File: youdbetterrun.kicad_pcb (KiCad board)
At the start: 4 copper layers, 60 x 53 mm, 51 parts, among them J1 GT-USB-7010ASV, J2 Conn_01x05_Pin, J3 Conn_01x10_Pin, J4 FH12A-24S-0.5SH(55), Q1 S8050, Q2 S8050, Q3 Q_NMOS_GSD, SW1 TS-1088R-02026, SW2 TS-1088R-02026, U1 CP2104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

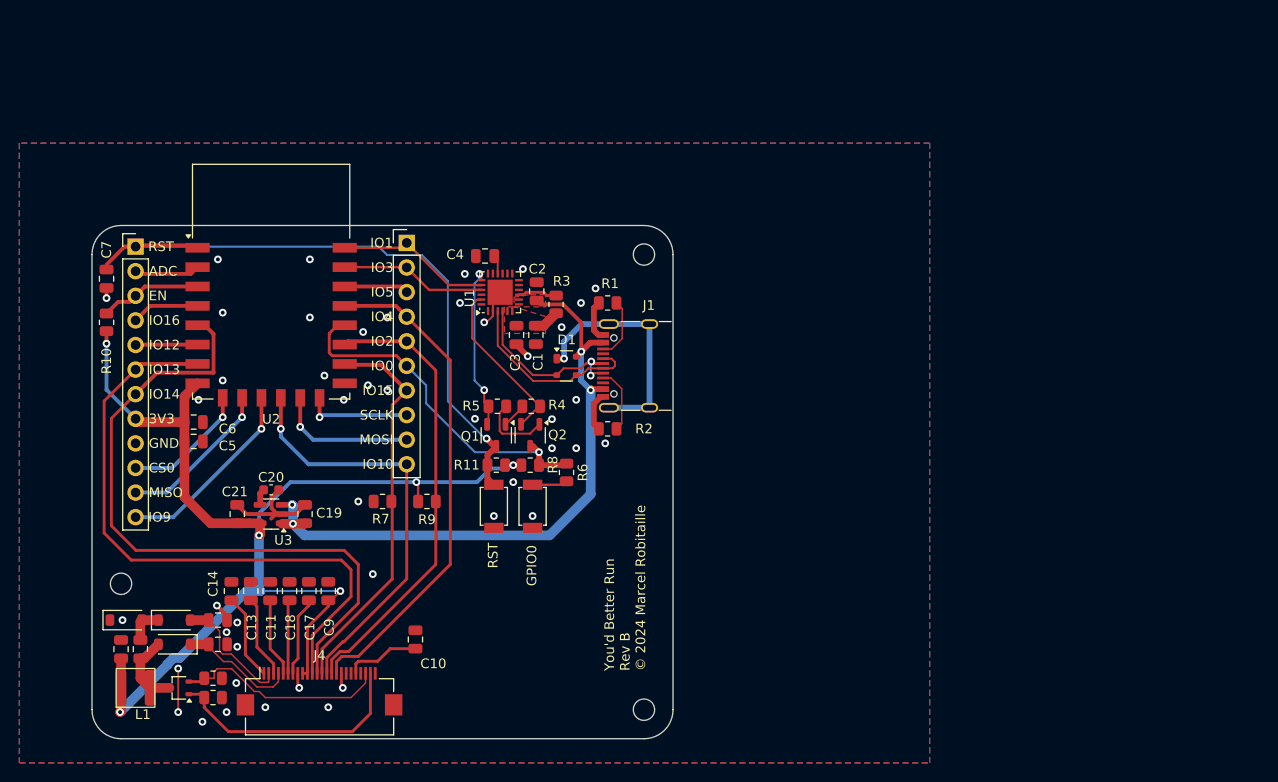
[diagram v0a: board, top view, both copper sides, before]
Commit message: Switch to ESP32
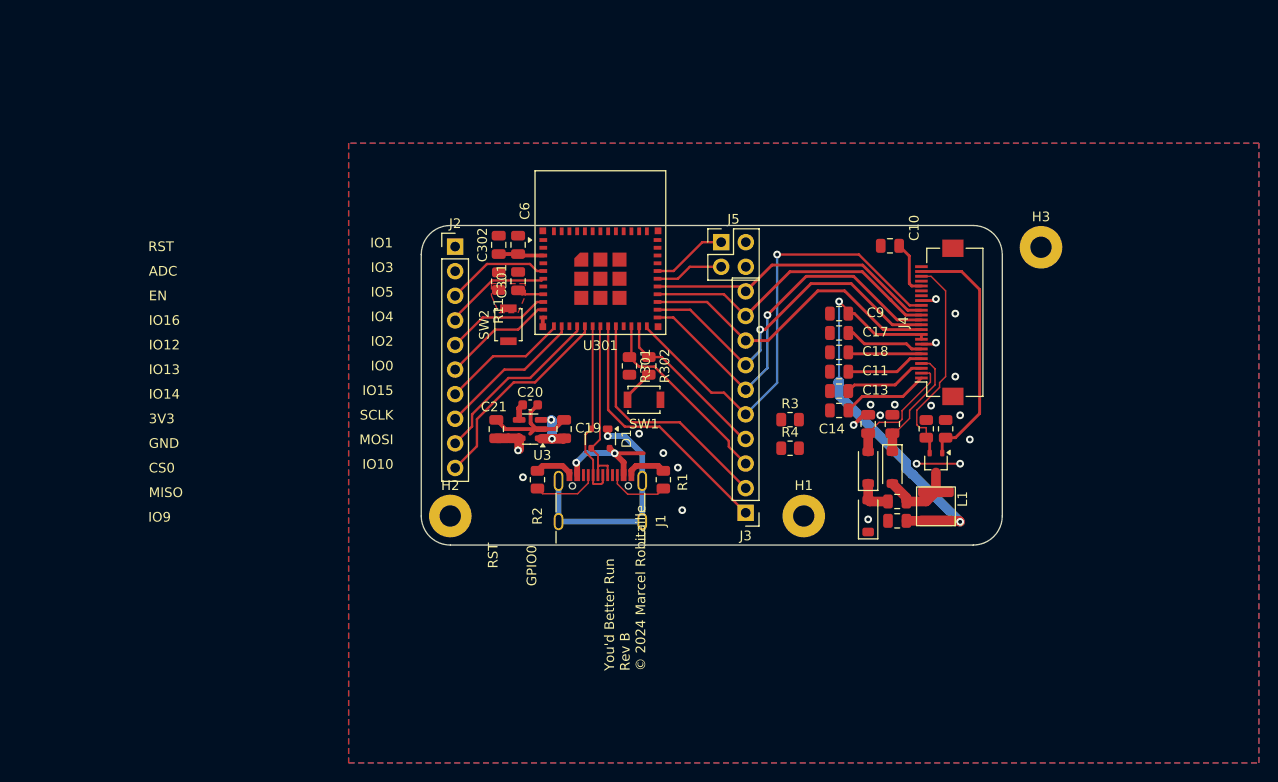
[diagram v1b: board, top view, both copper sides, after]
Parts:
- removed C1, C4: 4u7, Capacitor_SMD:C_0805_2012Metric
- removed C2, C3: 100n, Capacitor_SMD:C_0805_2012Metric
- removed C5: 10u, Capacitor_SMD:C_0805_2012Metric
- removed C7: 470p, Capacitor_SMD:C_0805_2012Metric
- removed Q1, Q2: S8050, Package_TO_SOT_SMD:SOT-23-3
- removed R10, R7, R8, R9: 10k, Resistor_SMD:R_0805_2012Metric
- removed R5: 12k, Resistor_SMD:R_0805_2012Metric
- removed R6: 470, Resistor_SMD:R_0805_2012Metric
- removed U1: CP2104, Package_DFN_QFN:QFN-24-1EP_4x4mm_P0.5mm_EP2.6x2.6mm
- removed U2: ESP-12F, RF_Module:ESP-12E
- added C301: 1u, Capacitor_SMD:C_0805_2012Metric, F.Cu at (136.5, 59.2)
- added C302: 22u, Capacitor_SMD:C_0805_2012Metric, F.Cu at (134.5, 55.5)
- added H1: MountingHole_Pad, MountingHole:MountingHole_2.2mm_M2_Pad, F.Cu at (166.0, 83.5)
- added H2: MountingHole_Pad, MountingHole:MountingHole_2.2mm_M2_Pad, F.Cu at (129.5, 83.5)
- added H3: MountingHole_Pad, MountingHole:MountingHole_2.2mm_M2_Pad, F.Cu at (190.5, 55.8)
- added J5: Conn_01x04, Connector_PinHeader_2.54mm:PinHeader_2x02_P2.54mm_Vertical, F.Cu at (157.5, 55.2)
- added R301: 10k, Resistor_SMD:R_0805_2012Metric, F.Cu at (148.0, 68.0)
- added R302: 470, Resistor_SMD:R_0805_2012Metric, F.Cu at (150.0, 68.0)
- added U301: ESP32-C6-MINI-1, RF_Module:ESP32-C6-MINI-1, F.Cu at (145.0, 59.0)
- J2: footprint Connector_PinHeader_2.54mm:PinHeader_1x12_P2.54mm_Vertical -> Connector_PinHeader_2.54mm:PinHeader_1x10_P2.54mm_Vertical
- R3: value 4k7 -> 2k2
- R4: value 12k -> 2k2
- SW1, SW2: value TS-1088R-02026 -> SWT0010-015016SSA; footprint youdbetterrun:TS-1088R-02026_SW_SMD_3x4mm -> youdbetterrun:SWT0010-015016SSA
- moved L1 84.8 mm to (179.7, 82.5), turned to 180 degrees
- moved Q3 81.5 mm to (179.7, 78.0), turned to -90 degrees
- moved C8 81.2 mm to (175.7, 84.0), turned to 180 degrees
- moved R12 80.6 mm to (180.7, 74.5), turned to 90 degrees
- moved C12 79.6 mm to (175.7, 82.0), turned to 0 degrees
- moved R13 78.0 mm to (178.7, 74.5), turned to 90 degrees
- moved D4 77.4 mm to (172.7, 83.5), turned to 90 degrees
- moved D2 76.4 mm to (175.2, 78.5), turned to -90 degrees
- moved J4 74.5 mm to (180.0, 63.5), turned to 90 degrees
- moved D3 73.4 mm to (172.7, 78.5), turned to 90 degrees
- moved C15 73.3 mm to (175.2, 74.0), turned to 90 degrees
- moved C16 70.1 mm to (172.7, 74.0), turned to 90 degrees
- moved C14 65.5 mm to (169.7, 72.6), turned to 180 degrees
- moved C13 64.2 mm to (169.7, 70.6), turned to 180 degrees
- moved C10 63.7 mm to (174.9, 55.6), turned to 180 degrees
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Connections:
- net /USB/D+ renamed /USB/USB_DP
- net /USB/D- renamed /USB/USB_DN
- J2 pad 1: /MCU/~{RST} -> GND
- J2 pad 10: /MCU/CS0 -> /MCU/IO7
- J2 pad 2: /MCU/ADC -> /EPD/3V3
- J2 pad 3: /MCU/EN -> /MCU/IO2
- J2 pad 4: /MCU/GPIO16 -> /MCU/IO3
- J2 pad 5: /MCU/GPIO12 -> /MCU/IO4
- J2 pad 6: /EPD/SPI.MOSI -> /MCU/IO5
- J2 pad 7: /EPD/SPI.SCLK -> /MCU/IO0
- J2 pad 8: /EPD/3V3 -> /MCU/IO1
- J2 pad 9: GND -> /MCU/IO6
- J3 pad 1: /MCU/TXD -> /MCU/IO14
- J3 pad 10: /EPD/EPD_D/C -> /EPD/EPD_RST
- J3 pad 2: /MCU/RXD -> /MCU/IO15
- J3 pad 3: /MCU/GPIO5 -> /MCU/IO8
- J3 pad 4: /EPD/EPD_BUSY -> /MCU/IO9
- J3 pad 5: /EPD/EPD_RST -> /EPD/EPD_BUSY
- J3 pad 6: /MCU/GPIO0 -> /EPD/SPI.~{CS}
- J3 pad 7: /EPD/SPI.~{CS} -> /EPD/SPI.SCLK
- J3 pad 8: /MCU/SCLK -> /EPD/SPI.MOSI
- J3 pad 9: /MCU/MOSI -> /EPD/EPD_D/C
- R11 pad 1: /MCU/~{RST} -> /MCU/EN
- R3 pad 1: /USB/VIO -> /EPD/3V3
- R3 pad 2: /USB/CP2104_~{RST} -> /MCU/SCL
- R4 pad 1: /USB/~{DTR} -> /EPD/3V3
- R4 pad 2: Net-(Q1-B) -> /MCU/SDA
- SW1 pad 1: Net-(R6-Pad1) -> GND
- SW1 pad 2: GND -> /MCU/BOOT9
- SW2 pad 2: /MCU/~{RST} -> /MCU/EN
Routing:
- net /EPD/3V3: track 122.2 -> 52.8 mm, vias 6 -> 3
- net /MCU/~{RST}: track 68.0 -> 0.00 mm, vias 1 -> 0
- net /USB/5V: track 67.0 -> 17.7 mm
- net /MCU/GPIO0: track 36.7 -> 0.00 mm, vias 1 -> 0
- net /EPD/SPI.SCLK: track 69.8 -> 36.1 mm, vias 0 -> 1
- net /EPD/SPI.MOSI: track 64.3 -> 32.7 mm
- net /MCU/IO14: track 0.00 -> 27.2 mm
- net /MCU/IO15: track 0.00 -> 25.2 mm
- net /MCU/IO7: track 0.00 -> 21.5 mm
- net /MCU/IO8: track 0.00 -> 20.2 mm
- net /MCU/GPIO9: track 20.0 -> 0.00 mm, vias 1 -> 0
- net /MCU/IO6: track 0.00 -> 18.6 mm
- net /USB/~{DTR}: track 17.3 -> 0.00 mm
- net /MCU/IO9: track 0.00 -> 17.2 mm
- net /USB/~{RTS}: track 17.1 -> 0.00 mm, vias 2 -> 0
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- added copper zone on F.Cu, net /MCU/EN
- removed copper zone on F.Cu, net /USB/5V
- removed copper zone on F.Cu, net /USB/VIO
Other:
- board size 60 x 53 mm -> 60 x 33 mm

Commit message: WIP
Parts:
- removed R301: 10k, Resistor_SMD:R_0805_2012Metric
- removed U301: ESP32-C6-MINI-1, RF_Module:ESP32-C6-MINI-1
- added J6: Conn_01x04, Connector_PinHeader_2.54mm:PinHeader_1x04_P2.54mm_Vertical, F.Cu at (182.2, 35.6)
- added U2: ESP32-S3-WROOM-1, RF_Module:ESP32-S3-WROOM-1, F.Cu at (145.6, 60.1)
- moved R302 13.3 mm to (156.0, 79.8)
- moved SW1 7.11 mm to (155.0, 76.0)
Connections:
- R302 pad 1: /MCU/IO9 -> Net-(U2-IO0)
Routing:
- net /MCU/IO14: track 27.2 -> 0.00 mm
- net /MCU/IO15: track 25.2 -> 0.00 mm
- net /MCU/IO7: track 21.5 -> 0.00 mm
- net /MCU/IO6: track 18.6 -> 0.00 mm
- net /MCU/IO8: track 20.2 -> 3.05 mm
- net /MCU/IO9: track 17.2 -> 0.34 mm
- net /MCU/IO1: track 15.3 -> 0.00 mm
- net /EPD/EPD_BUSY: track 49.0 -> 34.9 mm
- net /MCU/IO0: track 13.2 -> 0.00 mm
- net /EPD/SPI.~{CS}: track 40.3 -> 28.1 mm
- net /USB/USB_DP: track 18.1 -> 6.35 mm
- net /MCU/IO5: track 11.7 -> 0.00 mm
- net /EPD/SPI.SCLK: track 36.1 -> 24.7 mm
- net /MCU/IO3: track 11.1 -> 0.00 mm
- net /MCU/IO4: track 10.9 -> 0.00 mm
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
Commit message: WIP
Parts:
- removed R3, R4: 2k2, Resistor_SMD:R_0805_2012Metric
- removed U2: ESP32-S3-WROOM-1, RF_Module:ESP32-S3-WROOM-1
- added H4: MountingHole_Pad, MountingHole:MountingHole_2.2mm_M2_Pad, F.Cu at (130.0, 48.0)
- added J7: SM04B-SRSS-TB, Connector_JST:JST_SH_SM04B-SRSS-TB_1x04-1MP_P1.00mm_Horizontal, F.Cu at (154.0, 91.0)
- added J8: Conn_01x04, Connector_PinHeader_2.54mm:PinHeader_2x02_P2.54mm_Vertical, F.Cu at (129.7, 53.7)
- added R5: 10k, Resistor_SMD:R_0805_2012Metric, F.Cu at (140.0, 87.0)
- added R6: 10k, Resistor_SMD:R_0805_2012Metric, F.Cu at (142.0, 87.0)
- added U$30: , STEMMAQT, F.Cu at (143.3, 87.7)
- added U1: ESP32-C3-WROOM-02, RF_Module:ESP32-C3-WROOM-02, F.Cu at (133.8, 69.0)
- J2: footprint Connector_PinHeader_2.54mm:PinHeader_1x10_P2.54mm_Vertical -> Connector_PinHeader_2.54mm:PinHeader_1x07_P2.54mm_Vertical
- J3: footprint Connector_PinHeader_2.54mm:PinHeader_1x10_P2.54mm_Vertical -> Connector_PinHeader_2.54mm:PinHeader_1x03_P2.54mm_Vertical
- J6: value Conn_01x04 -> SM04B-SRSS-TB; footprint Connector_PinHeader_2.54mm:PinHeader_1x04_P2.54mm_Vertical -> Connector_JST:JST_SH_SM04B-SRSS-TB_1x04-1MP_P1.00mm_Horizontal
- moved J6 66.2 mm to (146.0, 91.0)
- moved J1 34.6 mm to (142.0, 48.5), turned to 180 degrees
- moved C302 32.8 mm to (130.0, 88.0), turned to 180 degrees
- moved R1 32.3 mm to (135.5, 51.7), turned to 90 degrees
- moved C6 31.2 mm to (130.0, 86.0), turned to 180 degrees
- moved R2 29.7 mm to (148.5, 51.7), turned to 90 degrees
- moved C301 28.9 mm to (133.8, 88.0), turned to 180 degrees
- moved SW2 28.3 mm to (135.0, 92.0)
- moved H3 27.6 mm to (164.0, 48.0)
- moved J2 27.3 mm to (130.0, 83.0), turned to 90 degrees
- moved R11 26.8 mm to (133.8, 86.0), turned to 180 degrees
- moved C21 26.7 mm to (153.5, 56.0), turned to -90 degrees
- moved SW1 22.6 mm to (139.0, 92.0), turned to 90 degrees
- moved U3 22.2 mm to (150.0, 56.0), turned to 0 degrees
- moved J3 20.0 mm to (145.0, 70.0), turned to 0 degrees
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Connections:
- J2 pad 1: GND -> /EPD/3V3
- J2 pad 2: /EPD/3V3 -> /MCU/EN
- J2 pad 3: /MCU/IO2 -> /MCU/IO5
- J2 pad 4: /MCU/IO3 -> /MCU/IO8
- J2 pad 5: /MCU/IO4 -> /MCU/IO9
- J2 pad 6: /MCU/IO5 -> GND
- J2 pad 7: /MCU/IO0 -> /MCU/IO10
- J3 pad 1: /MCU/IO14 -> /EPD/SPI.~{CS}
- J3 pad 2: /MCU/IO15 -> /EPD/SPI.SCLK
- J3 pad 3: /MCU/IO8 -> /EPD/SPI.MOSI
- J6 pad 1: /EPD/3V3 -> /MCU/IO9
- J6 pad 2: /MCU/SDA -> /MCU/IO8
- J6 pad 3: /MCU/SCL -> /EPD/3V3
- R302 pad 1: Net-(U2-IO0) -> /MCU/IO9
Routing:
- net /MCU/TXD: track 0.00 -> 34.0 mm, vias 0 -> 2
- net /MCU/RXD: track 0.00 -> 33.5 mm, vias 0 -> 2
- net /MCU/IO8: track 3.05 -> 31.9 mm
- net /MCU/IO9: track 0.34 -> 27.8 mm
- net /MCU/IO10: track 0.00 -> 26.2 mm, vias 0 -> 1
- net /EPD/EPD_D/C: track 22.2 -> 43.4 mm
- net /EPD/SPI.MOSI: track 21.9 -> 38.1 mm
- net /EPD/EPD_RST: track 22.4 -> 38.2 mm
- net /EPD/SPI.SCLK: track 24.7 -> 40.4 mm, vias 1 -> 0
- net /MCU/EN: track 0.00 -> 14.9 mm
- net /EPD/3V3: track 50.1 -> 36.4 mm, vias 3 -> 22
- net GND: track 30.5 -> 42.4 mm, vias 19 -> 79
- net /USB/USB_DP: track 6.35 -> 16.8 mm
- net /EPD/SPI.~{CS}: track 28.1 -> 37.7 mm, vias 1 -> 2
- net /USB/USB_DN: track 8.08 -> 16.8 mm
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- added copper zone on B.Cu, net /EPD/3V3
- added copper zone on F.Cu, net /EPD/3V3
- added copper zone on B.Cu, net /USB/5V
- added copper zone on F.Cu, net /USB/5V
- removed copper zone on F.Cu, net /MCU/EN
- removed copper zone on B.Cu, net GND
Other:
- board size 60 x 33 mm -> 40 x 50 mm
- board text added: "BOOT"
- board text added: "CLK"
- board text added: "CS"
- board text added: "IO8"
- board text added: "RXD"
- board text added: "TXD"
- board text added: "You'd Better Run!"
- board text added: "© 2025 Marcel Robitaille Rev C"
- board text removed: "ADC"
- board text removed: "CS0"
- board text removed: "GPIO0"
- board text removed: "IO12"
- board text removed: "IO13"
- board text removed: "IO14"
- board text removed: "IO15"
- board text removed: "IO16"
- board text removed: "IO4"
- board text removed: "MISO"
- board text removed: "SCLK"
- board text removed: "You'd Better Run Rev B © 2024 Marcel Robitaille"

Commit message: Fixes
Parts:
- removed U$30: , STEMMAQT
- added R3: 10k, Resistor_SMD:R_0805_2012Metric, F.Cu at (135.5, 56.0)
- added StemmaQTLogo: , STEMMAQT, F.Cu at (143.0, 87.7)
- U1: footprint RF_Module:ESP32-C3-WROOM-02 -> youdbetterrun:ESP32-C3-WROOM-02_big_vias
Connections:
- J6 pad MP: (no net) -> GND
- J7 pad MP: (no net) -> GND
- J8 pad 2: /MCU/IO3 -> /MCU/IO2
- U1 pad 15: /MCU/IO3 -> /EPD/EPD_BUSY
- U1 pad 16: /EPD/EPD_BUSY -> /MCU/IO2
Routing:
- net /MCU/IO2: track 0.00 -> 10.8 mm
- net /MCU/IO3: track 7.46 -> 0.00 mm
- net /EPD/3V3: track 36.4 -> 37.9 mm, vias 22 -> 23
- net /EPD/EPD_BUSY: track 36.2 -> 34.7 mm
- net GND: vias 79 -> 81
